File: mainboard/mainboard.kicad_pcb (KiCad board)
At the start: 2 copper layers, 88.9 x 88.9 mm, 48 parts, among them SW1 SW_DPDT_x2, U1 74AC04, U2 AS6C4008, U3 74AC32, U4 74AC00, U5 SST39SF040, U6 NE555, U7 74HC245, U9 74HC574, Y1 Crystal

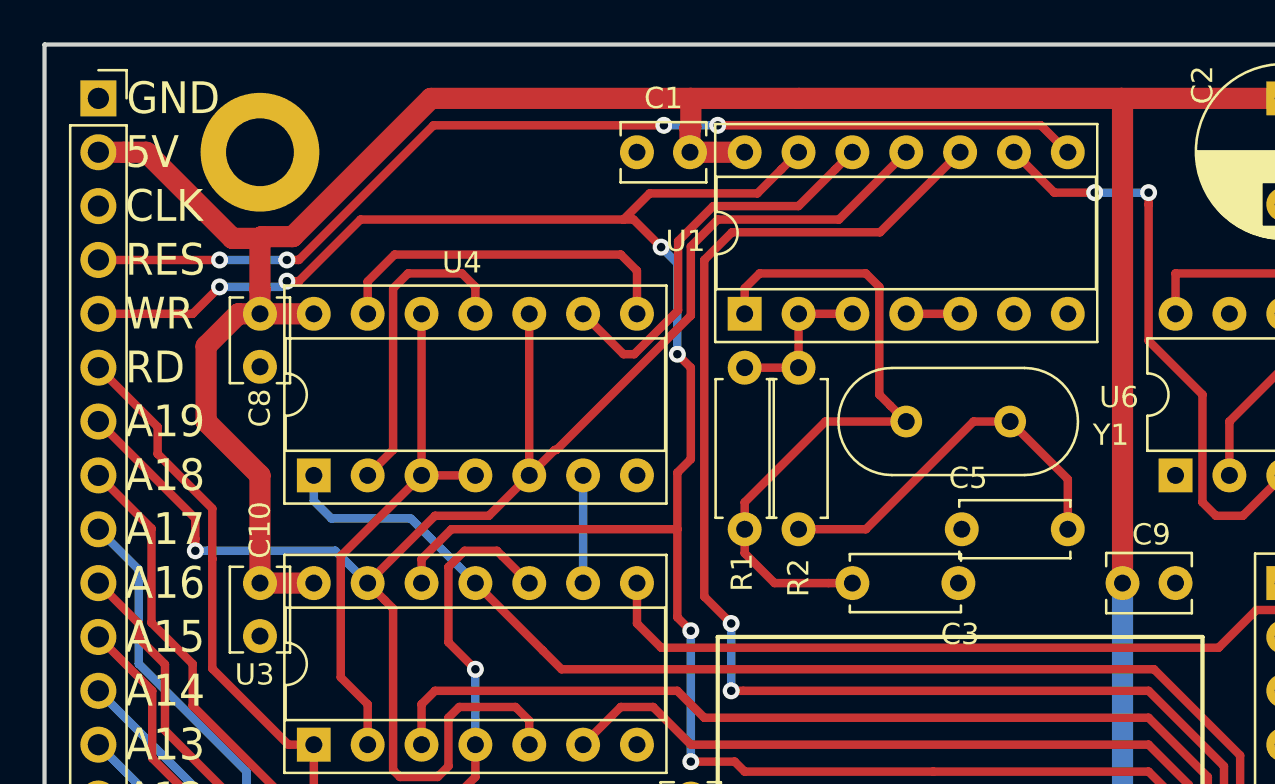
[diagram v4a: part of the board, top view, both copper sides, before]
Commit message: Rename A19 to RAM to create two distinct address spaces.
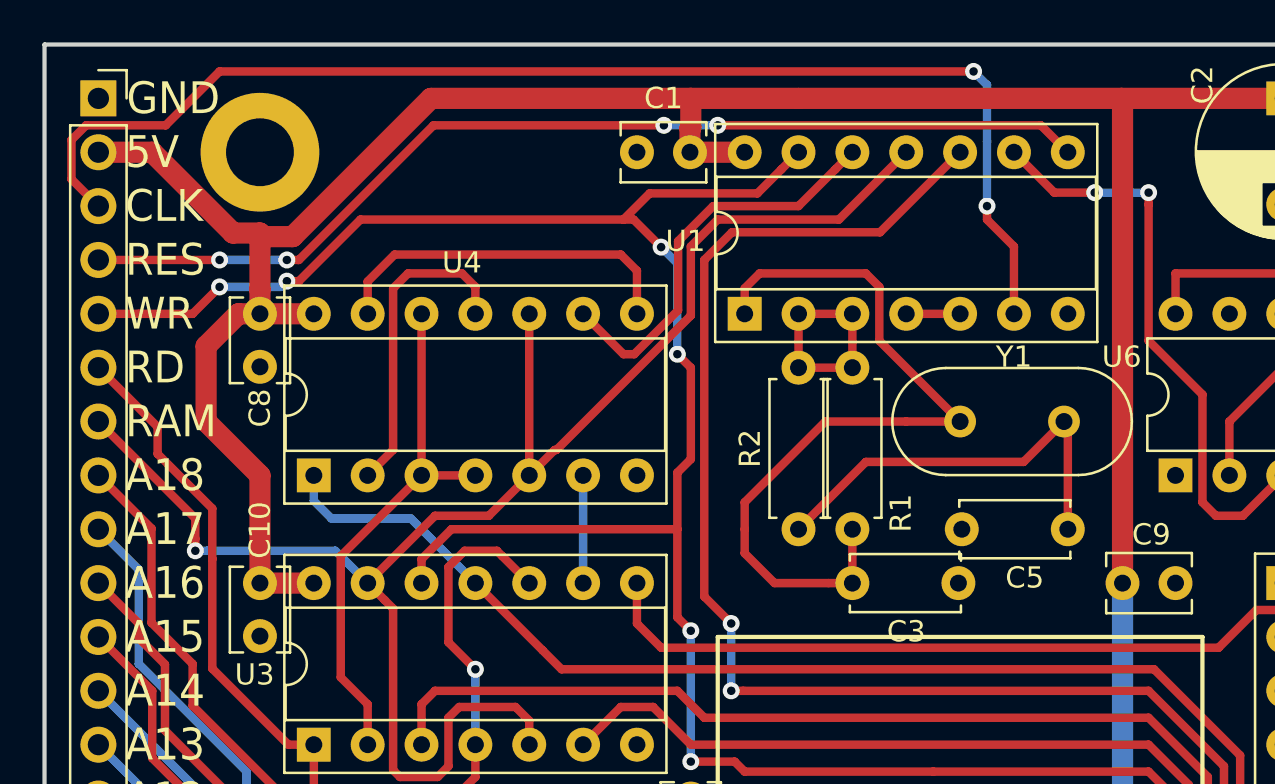
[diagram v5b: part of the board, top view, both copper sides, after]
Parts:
- U1: value 74AC04 -> 74HC04
- moved R1 5.08 mm to (101.6, 63.5)
- moved Y1 2.54 mm to (106.7, 66.0)
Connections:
- net /A19 renamed /RAM
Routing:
- net /CLK: track 0.00 -> 59.7 mm, vias 0 -> 2
- net Net-(C3-Pad1): track 32.2 -> 38.0 mm
- net Net-(R1-Pad1): track 7.62 -> 10.2 mm
- net Net-(C5-Pad1): track 18.3 -> 19.8 mm
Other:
- board text added: "RAM"
- board text removed: "A19"

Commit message: Switch meaning of the A19 pin from RAM to ROM. Use pull-ups instead of pull-downs for the input port.
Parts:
- RN1: value 22k -> 10k
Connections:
- net /RD renamed /RD#
- net /RES renamed /RES#
- net /WR renamed /WR#
- JBUS1 pad 7: /RAM -> /ROM
- RN1 pad 1: GND -> +5V
- U1 pad 10: /CERAM -> /RAM
- U1 pad 11: /RAM -> /ROM
- U2 pad 22: /CERAM -> /ROM
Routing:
- net /CERAM: track 116.1 -> 0.00 mm, vias 2 -> 0
- net /ROM: track 0.00 -> 114.3 mm, vias 0 -> 4
- net /RAM: track 80.1 -> 64.7 mm, vias 1 -> 0
- net +5V: track 269.0 -> 272.8 mm
- net Net-(U1-Pad12): track 19.3 -> 18.2 mm
- net /WR#: track 137.6 -> 136.8 mm
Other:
- board text added: "RD#"
- board text added: "RES#"
- board text added: "ROM"
- board text added: "WR#"
- board text removed: "RAM"
- board text removed: "RD"
- board text removed: "RES"
- board text removed: "WR"

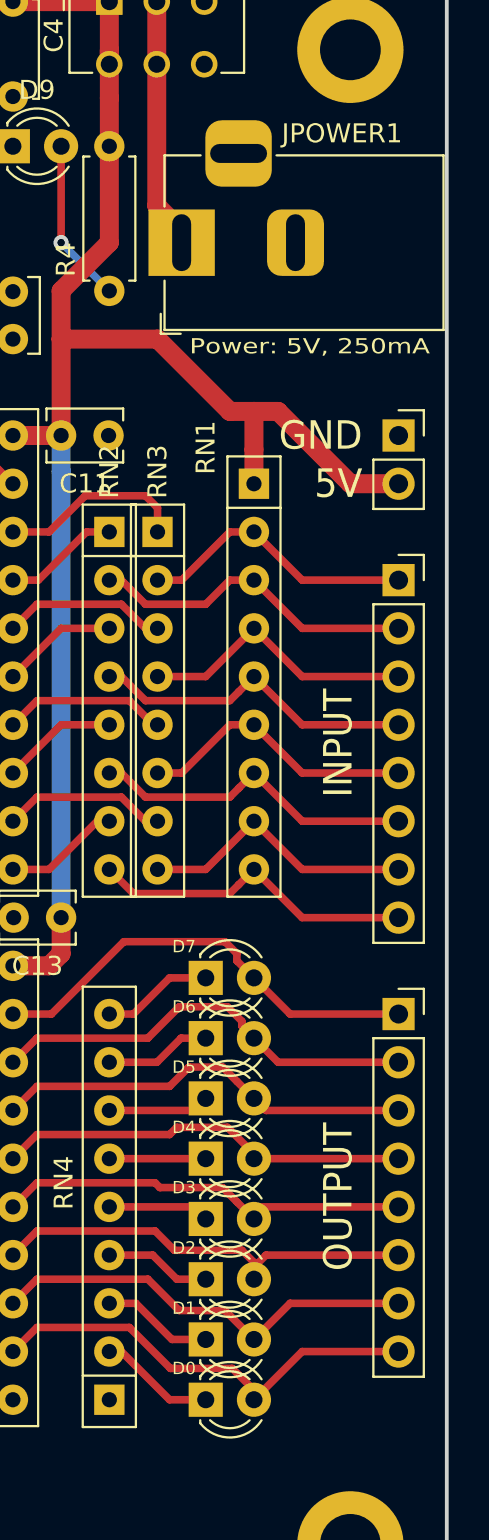
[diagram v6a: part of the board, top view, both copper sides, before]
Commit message: Add power input on pin header to allow USB device to drive the machine.
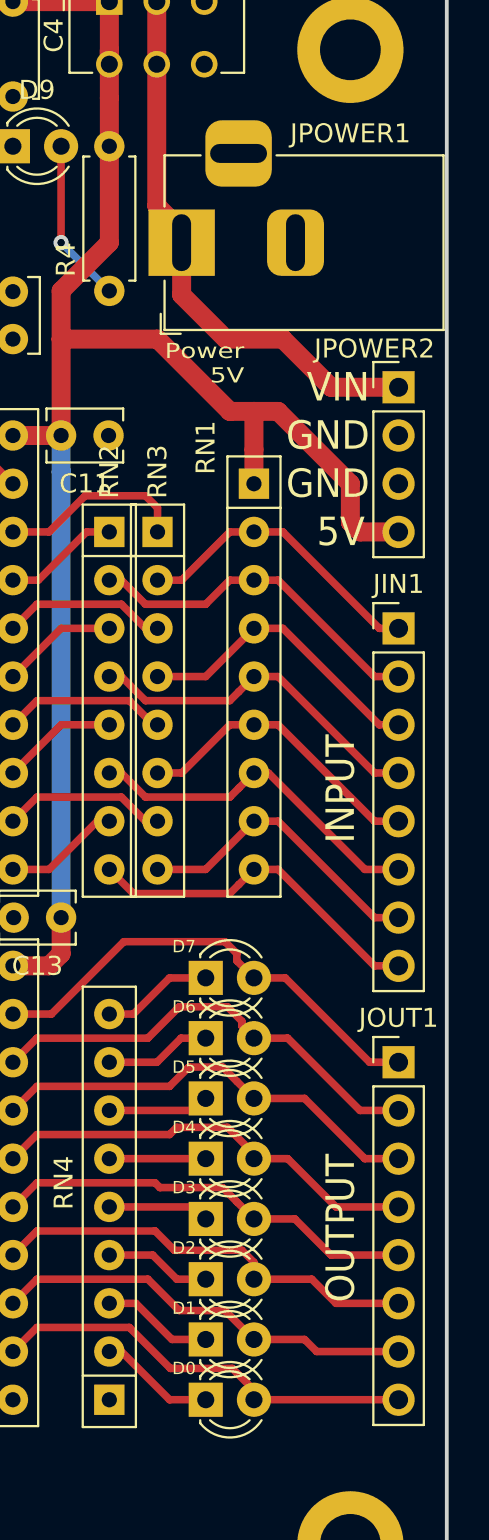
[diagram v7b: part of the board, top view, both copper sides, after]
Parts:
- removed JIOPOWER1: Conn_01x02_Female, Connector_PinSocket_2.54mm:PinSocket_1x02_P2.54mm_Vertical
- added JPOWER2: Conn_01x04_Male, Connector_PinHeader_2.54mm:PinHeader_1x04_P2.54mm_Vertical, F.Cu at (149.9, 71.1)
- JIN1, JOUT1: value Conn_01x08_Female -> Conn_01x08_Male; footprint Connector_PinSocket_2.54mm:PinSocket_1x08_P2.54mm_Vertical -> Connector_PinHeader_2.54mm:PinHeader_1x08_P2.54mm_Vertical
- moved JOUT1 2.54 mm to (149.9, 106.7)
- moved JIN1 2.54 mm to (149.9, 83.8)
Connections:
- net Net-(JPOWER1-Pad1) renamed /VIN
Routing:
- net /VIN: track 13.2 -> 29.4 mm
- net +5V: track 272.8 -> 275.1 mm
- net Net-(JIN1-Pad3): track 14.8 -> 15.9 mm
- net Net-(D5-Pad2): track 22.2 -> 23.3 mm
- net Net-(JIN1-Pad7): track 14.8 -> 15.9 mm
- net Net-(JIN1-Pad5): track 14.8 -> 15.9 mm
- net Net-(JIN1-Pad2): track 17.3 -> 18.4 mm
- net Net-(D7-Pad2): track 23.7 -> 24.8 mm
- net Net-(JIN1-Pad1): track 14.8 -> 15.9 mm
- net Net-(JIN1-Pad6): track 17.3 -> 18.4 mm
- net Net-(D4-Pad2): track 21.9 -> 23.0 mm
- net Net-(D0-Pad2): track 23.8 -> 22.7 mm
- net Net-(JIN1-Pad8): track 17.3 -> 18.4 mm
- net Net-(JIN1-Pad4): track 17.3 -> 18.4 mm
- net Net-(D6-Pad2): track 22.9 -> 23.9 mm
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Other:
- board text added: "Power 5V"
- board text added: "VIN"
- board text removed: "Power: 5V, 250mA"

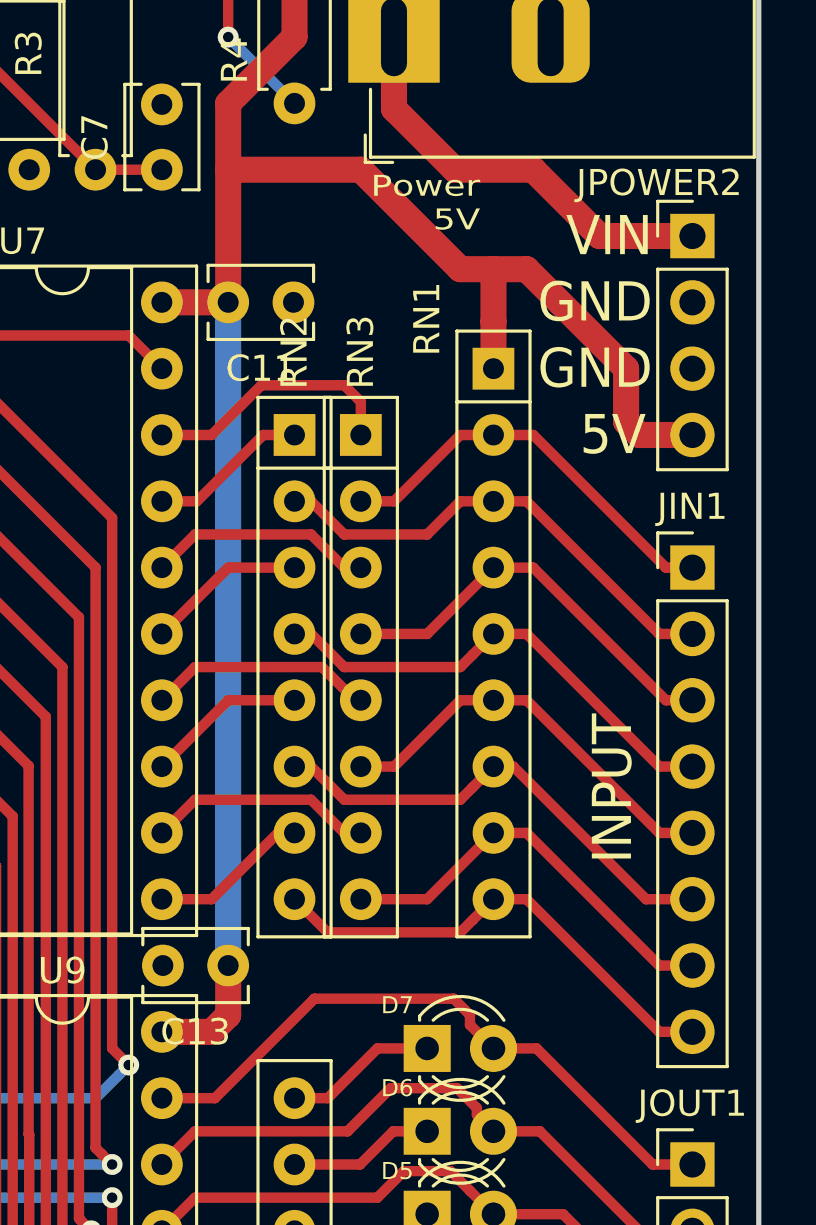
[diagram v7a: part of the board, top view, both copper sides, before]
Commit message: Remove protection resistors for input port. Stagger ports so an IO board will have better mechanical stability
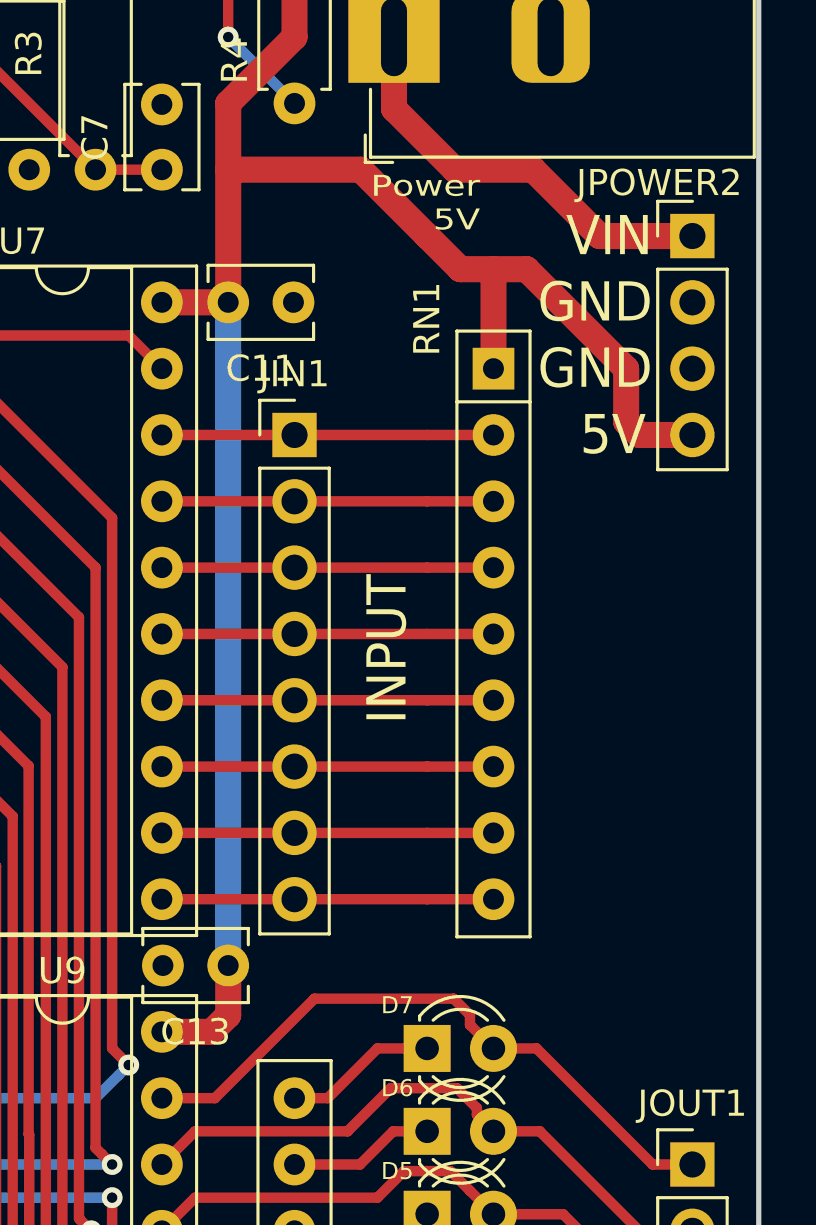
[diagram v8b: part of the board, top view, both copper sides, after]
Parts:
- removed RN2, RN3: 1k, Resistor_THT:R_Array_SIP8
- moved JIN1 16.1 mm to (134.6, 78.7)
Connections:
- U7 pad 11: Net-(RN2-Pad7) -> Net-(JIN1-Pad8)
- U7 pad 12: Net-(RN3-Pad7) -> Net-(JIN1-Pad7)
- U7 pad 13: Net-(RN2-Pad5) -> Net-(JIN1-Pad6)
- U7 pad 14: Net-(RN3-Pad5) -> Net-(JIN1-Pad5)
- U7 pad 15: Net-(RN2-Pad3) -> Net-(JIN1-Pad4)
- U7 pad 16: Net-(RN3-Pad3) -> Net-(JIN1-Pad3)
- U7 pad 17: Net-(RN2-Pad1) -> Net-(JIN1-Pad2)
- U7 pad 18: Net-(RN3-Pad1) -> Net-(JIN1-Pad1)
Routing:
- net Net-(RN3-Pad1): track 9.94 -> 0.00 mm
- net Net-(RN3-Pad7): track 8.67 -> 0.00 mm
- net Net-(RN3-Pad5): track 8.67 -> 0.00 mm
- net Net-(RN3-Pad3): track 8.67 -> 0.00 mm
- net Net-(RN2-Pad1): track 6.13 -> 0.00 mm
- net Net-(RN2-Pad3): track 6.13 -> 0.00 mm
- net Net-(RN2-Pad7): track 6.13 -> 0.00 mm
- net Net-(RN2-Pad5): track 6.13 -> 0.00 mm
- net Net-(JIN1-Pad8): track 18.4 -> 12.7 mm
- net Net-(JIN1-Pad6): track 18.4 -> 12.7 mm
- net Net-(JIN1-Pad4): track 18.4 -> 12.7 mm
- net Net-(JIN1-Pad2): track 18.4 -> 12.7 mm
- net Net-(JIN1-Pad3): track 15.9 -> 12.7 mm
- net Net-(JIN1-Pad1): track 15.9 -> 12.7 mm
- net Net-(JIN1-Pad5): track 15.9 -> 12.7 mm
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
